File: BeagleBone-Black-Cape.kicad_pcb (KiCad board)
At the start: 4 copper layers, 61.9 x 92.1 mm, 77 parts, among them J501 Conn_ARM_JTAG_SWD_10, J502 3.3V, P101 BeagleBone_Black_Header, P102 BeagleBone_Black_Header, U401 LM3671, U601 cc1352p, U602 MX25R8035FZUIL0, Y601 32.768kHz, Y602 48MHz

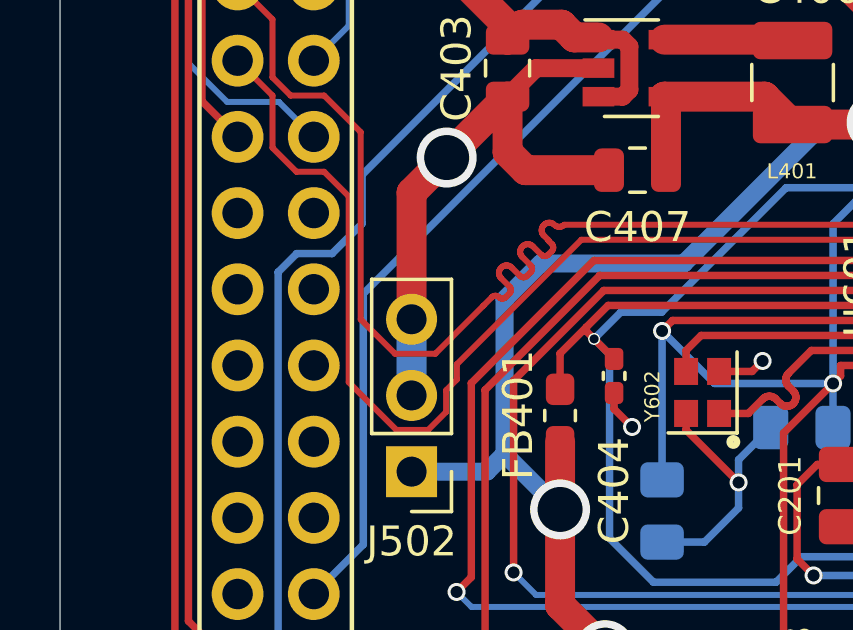
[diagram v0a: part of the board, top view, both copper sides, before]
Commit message: Made ZNP_RX trace prettier
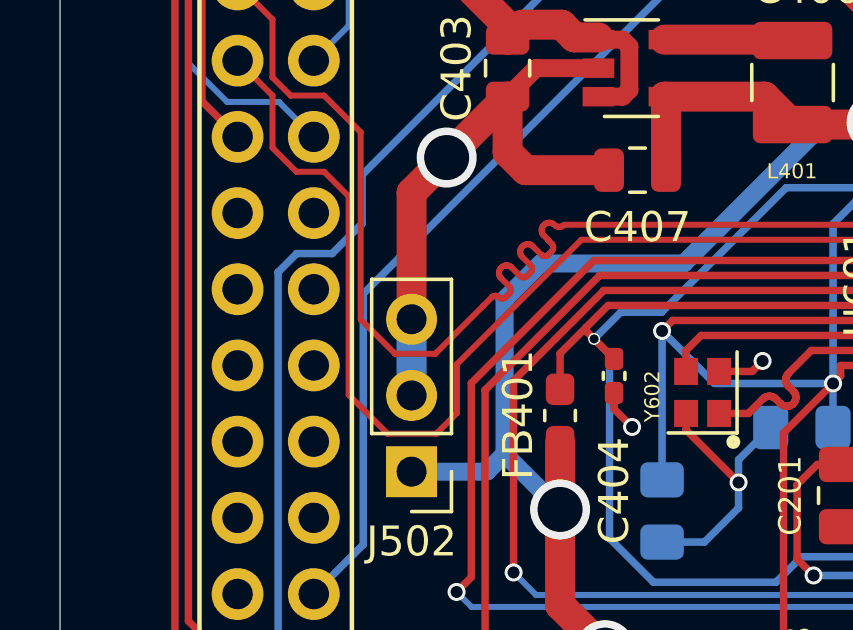
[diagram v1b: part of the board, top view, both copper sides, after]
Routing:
- net ZNP_RX: track 49.8 -> 50.3 mm
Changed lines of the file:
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@@
     (thickness 1.6)
     (drawings 22)
-    (tracks 923)
+    (tracks 921)
     (zones 0)
     (modules 77)
@@
   (segment (start 141.5201 126.6824) (end 144.4701 126.6824) (width 1) (layer F.Cu) (net 26) (status 30))
   (segment (start 152.6451 126.7074) (end 155.5951 126.7074) (width 1) (layer F.Cu) (net 26) (status 30))
-  (segment (start 127.8301 83.5924) (end 137.4401 83.5924) (width 0.2) (layer F.Cu) (net 8))
-  (segment (start 117.533701 78.786001) (end 117.533701 80.526001) (width 0.2) (layer F.Cu) (net 8))
-  (segment (start 120.073701 88.340929) (end 121.665173 89.932401) (width 0.2) (layer F.Cu) (net 8))
-  (segment (start 123.6801 87.7424) (end 127.8301 83.5924) (width 0.2) (layer F.Cu) (net 8))
-  (segment (start 117.533701 80.526001) (end 118.333701 81.326001) (width 0.2) (layer F.Cu) (net 8))
-  (segment (start 116.3701 77.6224) (end 117.533701 78.786001) (width 0.2) (layer F.Cu) (net 8) (status 10))
-  (segment (start 119.255831 81.326001) (end 120.073701 82.143871) (width 0.2) (layer F.Cu) (net 8))
-  (segment (start 122.722101 89.932401) (end 123.320101 89.334401) (width 0.2) (layer F.Cu) (net 8))
-  (segment (start 118.333701 81.326001) (end 119.255831 81.326001) (width 0.2) (layer F.Cu) (net 8))
-  (segment (start 120.073701 82.143871) (end 120.073701 88.340929) (width 0.2) (layer F.Cu) (net 8))
-  (segment (start 121.665173 89.932401) (end 122.722101 89.932401) (width 0.2) (layer F.Cu) (net 8))
-  (segment (start 123.320101 88.611345) (end 123.6801 88.251346) (width 0.2) (layer F.Cu) (net 8))
-  (segment (start 123.320101 89.334401) (end 123.320101 88.611345) (width 0.2) (layer F.Cu) (net 8))
-  (segment (start 123.6801 88.251346) (end 123.6801 87.7424) (width 0.2) (layer F.Cu) (net 8))
   (segment (start 146.558102 86.394398) (end 146.558102 85.454398) (width 0.25) (layer B.Cu) (net 8))
   (segment (start 137.4401 85.477402) (end 140.395098 88.4324) (width 0.25) (layer B.Cu) (net 8))
@@
   (segment (start 146.705099 85.307401) (end 146.7301 85.307401) (width 0.25) (layer B.Cu) (net 8))
   (segment (start 137.4401 85.477402) (end 137.4401 83.617401) (width 0.25) (layer B.Cu) (net 8))
+  (segment (start 123.6801 87.7424) (end 127.8301 83.5924) (width 0.2) (layer F.Cu) (net 8))
+  (segment (start 122.9951 90.0574) (end 123.6801 89.3724) (width 0.2) (layer F.Cu) (net 8))
+  (segment (start 121.3701 90.0574) (end 122.9951 90.0574) (width 0.2) (layer F.Cu) (net 8))
+  (segment (start 127.8301 83.5924) (end 137.4401 83.5924) (width 0.2) (layer F.Cu) (net 8))
+  (segment (start 120.073701 88.761001) (end 121.3701 90.0574) (width 0.2) (layer F.Cu) (net 8))
+  (segment (start 119.255831 81.326001) (end 120.073701 82.143871) (width 0.2) (layer F.Cu) (net 8))
+  (segment (start 120.073701 82.143871) (end 120.073701 88.761001) (width 0.2) (layer F.Cu) (net 8))
+  (segment (start 118.333701 81.326001) (end 119.255831 81.326001) (width 0.2) (layer F.Cu) (net 8))
+  (segment (start 123.6801 89.3724) (end 123.6801 87.7424) (width 0.2) (layer F.Cu) (net 8))
+  (segment (start 117.533701 80.526001) (end 118.333701 81.326001) (width 0.2) (layer F.Cu) (net 8))
+  (segment (start 117.533701 78.786001) (end 117.533701 80.526001) (width 0.2) (layer F.Cu) (net 8))
+  (segment (start 116.3701 77.6224) (end 117.533701 78.786001) (width 0.2) (layer F.Cu) (net 8))
   (via (at 146.7301 84.7824) (size 0.4) (drill 0.3) (layers F.Cu B.Cu) (net 152))
   (segment (start 145.3576 84.7824) (end 146.7301 84.7824) (width 0.2) (layer F.Cu) (net 152) (status 10))

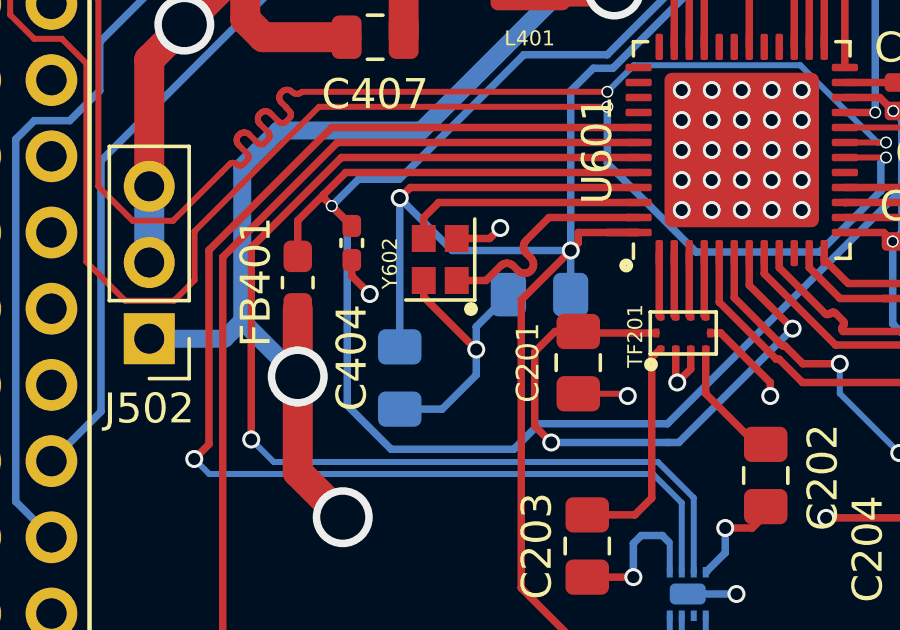
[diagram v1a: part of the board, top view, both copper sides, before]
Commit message: undid the Y602 Pad thing after crossreferencing datasheet
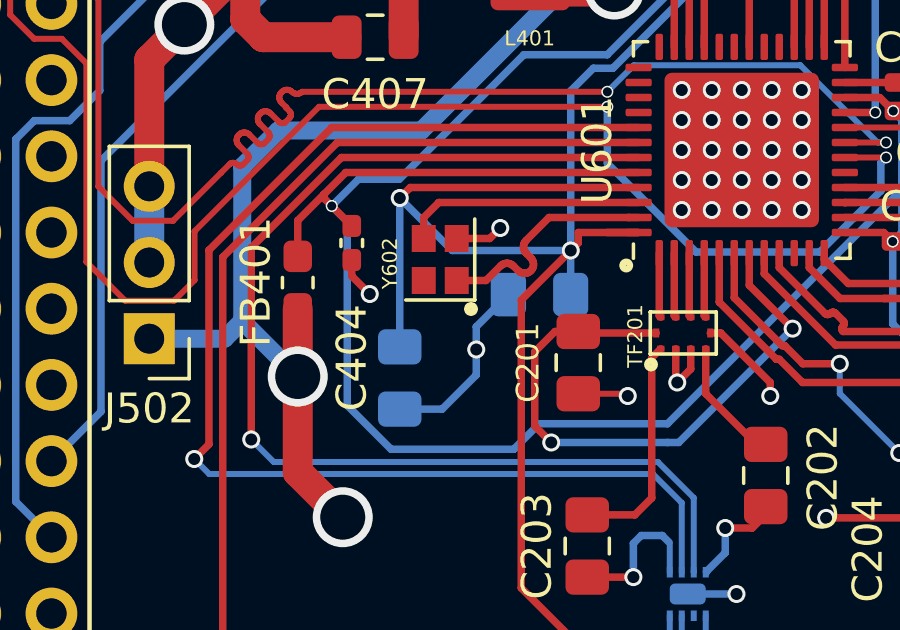
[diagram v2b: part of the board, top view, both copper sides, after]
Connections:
- Y602 pad 4: GND -> (no net)
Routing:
- net GND: track 182.1 -> 179.0 mm
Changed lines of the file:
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@@
     (thickness 1.6)
     (drawings 22)
-    (tracks 921)
+    (tracks 919)
     (zones 0)
     (modules 77)
@@
       (effects (font (size 0.5 0.5) (thickness 0.075)))
     )
-    (pad 4 smd rect (at -0.7 -0.55 90) (size 0.9 0.8) (layers F.Cu F.Paste F.Mask)
-      (net 26 GND))
+    (pad 4 smd rect (at -0.7 -0.55 90) (size 0.9 0.8) (layers F.Cu F.Paste F.Mask))
     (pad 3 smd rect (at 0.7 -0.55 90) (size 0.9 0.8) (layers F.Cu F.Paste F.Mask)
       (net 33 X48M_N))
@@
   (segment (start 116.3701 115.7224) (end 118.9101 115.7224) (width 1) (layer F.Cu) (net 26) (status 30))
   (segment (start 116.3701 118.2624) (end 118.9101 118.2624) (width 1) (layer F.Cu) (net 26) (status 30))
-  (segment (start 131.3201 89.9324) (end 133.0701 91.6824) (width 0.25) (layer F.Cu) (net 26))
-  (segment (start 131.3201 89.3824) (end 131.3201 89.9324) (width 0.25) (layer F.Cu) (net 26))
   (segment (start 138.3251 82.2074) (end 137.4401 83.0924) (width 0.2) (layer B.Cu) (net 152))
   (segment (start 143.872258 82.2074) (end 138.3251 82.2074) (width 0.2) (layer B.Cu) (net 152))

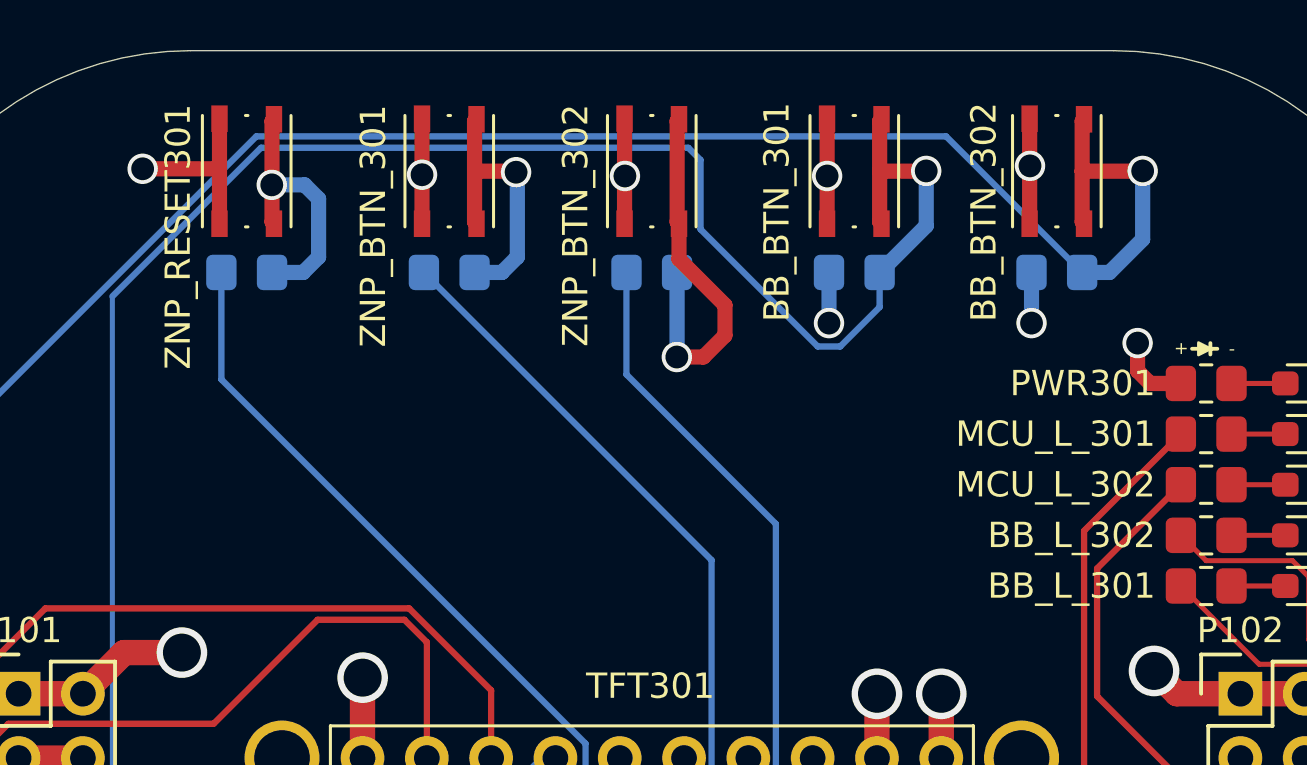
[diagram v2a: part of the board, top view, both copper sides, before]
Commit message: Fixed silkscreens for buttons and LEDs
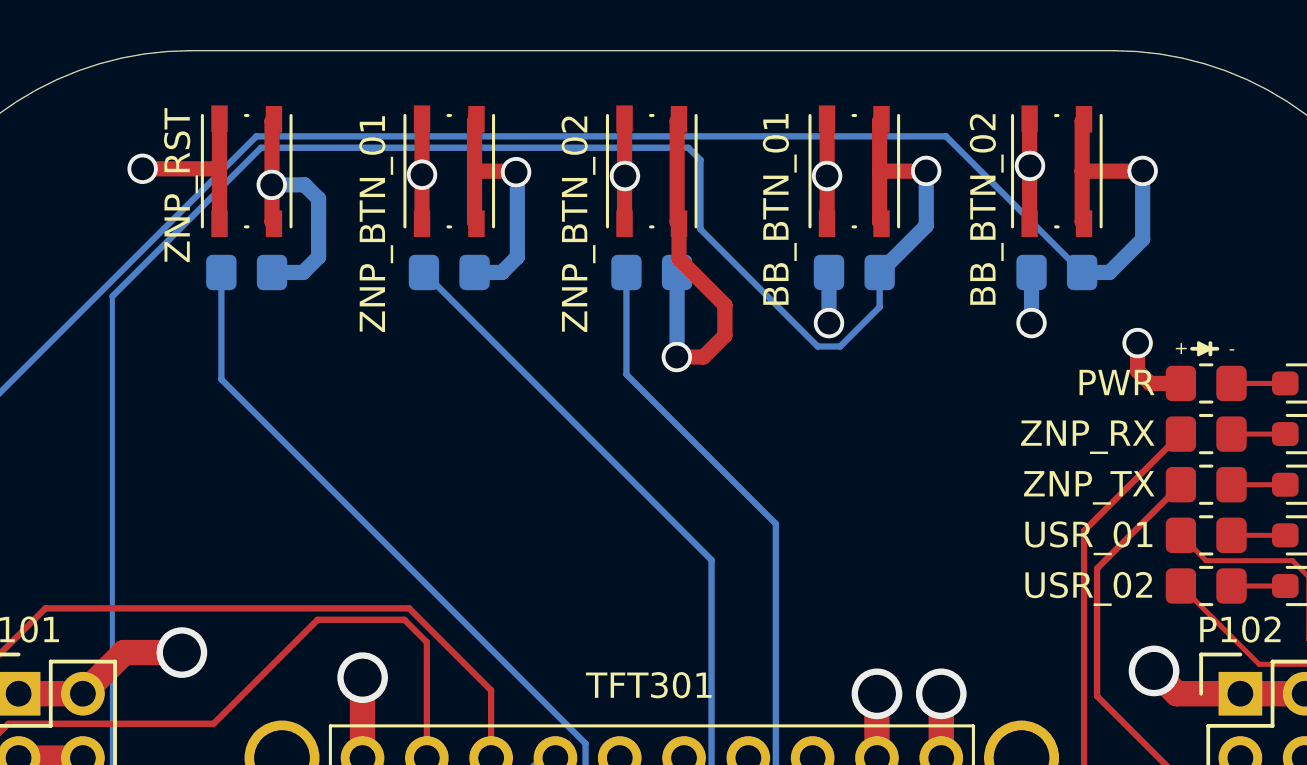
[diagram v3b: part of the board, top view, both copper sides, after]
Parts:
- renumbered BB_BTN_301 to BB_BTN_01, BB_BTN_302 to BB_BTN_02, PWR301 to PWR, BB_L_302 to USR_01, BB_L_301 to USR_02, ZNP_BTN_301 to ZNP_BTN_01, ZNP_BTN_302 to ZNP_BTN_02, ZNP_RESET301 to ZNP_RST, MCU_L_301 to ZNP_RX, MCU_L_302 to ZNP_TX
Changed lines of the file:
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@@
     (tags "tactile switch Wurth Wuerth")
     (attr smd)
-    (fp_text reference ZNP_BTN_302 (at -2.14 -3.01 90) (layer F.SilkS)
-      (effects (font (size 1 1) (thickness 0.15)))
+    (fp_text reference ZNP_BTN_02 (at -6.415 -3.01 90) (layer F.SilkS)
+      (effects (font (size 1 1) (thickness 0.15)) (justify left))
     )
     (fp_text value SW_Push (at 0 2.55 90) (layer F.Fab)
@@
     (tags "tactile switch Wurth Wuerth")
     (attr smd)
-    (fp_text reference ZNP_BTN_301 (at -2.165 -3 90) (layer F.SilkS)
-      (effects (font (size 1 1) (thickness 0.15)))
+    (fp_text reference ZNP_BTN_01 (at -6.415 -3 90) (layer F.SilkS)
+      (effects (font (size 1 1) (thickness 0.15)) (justify left))
     )
     (fp_text value SW_Push (at 0 2.55 90) (layer F.Fab)
@@
     (tags "tactile switch Wurth Wuerth")
     (attr smd)
-    (fp_text reference BB_BTN_302 (at -1.615 -2.885 90) (layer F.SilkS)
-      (effects (font (size 1 1) (thickness 0.15)))
+    (fp_text reference BB_BTN_02 (at -5.415 -2.885 90) (layer F.SilkS)
+      (effects (font (size 1 1) (thickness 0.15)) (justify left))
     )
     (fp_text value SW_Push (at 0 2.55 90) (layer F.Fab)
@@
     (tags "tactile switch Wurth Wuerth")
     (attr smd)
-    (fp_text reference BB_BTN_301 (at -1.615 -3.06 90) (layer F.SilkS)
-      (effects (font (size 1 1) (thickness 0.15)))
+    (fp_text reference BB_BTN_01 (at -5.415 -3.06 90) (layer F.SilkS)
+      (effects (font (size 1 1) (thickness 0.15)) (justify left))
     )
     (fp_text value SW_Push (at 0 2.55 90) (layer F.Fab)
@@
     (tags "LED handsolder")
     (attr smd)
-    (fp_text reference PWR301 (at 6 0) (layer F.SilkS)
+    (fp_text reference PWR (at 6 0) (layer F.SilkS)
       (effects (font (size 1 1) (thickness 0.15)) (justify right))
     )
@@
     (tags "LED handsolder")
     (attr smd)
-    (fp_text reference MCU_L_302 (at 6 0) (layer F.SilkS)
+    (fp_text reference ZNP_TX (at 6 0) (layer F.SilkS)
       (effects (font (size 1 1) (thickness 0.15)) (justify right))
     )
@@
     (tags "LED handsolder")
     (attr smd)
-    (fp_text reference MCU_L_301 (at 6 0) (layer F.SilkS)
+    (fp_text reference ZNP_RX (at 6 0) (layer F.SilkS)
       (effects (font (size 1 1) (thickness 0.15)) (justify right))
     )
@@
     (tags "LED handsolder")
     (attr smd)
-    (fp_text reference BB_L_302 (at 6 0) (layer F.SilkS)
+    (fp_text reference USR_01 (at 6 0) (layer F.SilkS)
       (effects (font (size 1 1) (thickness 0.15)) (justify right))
     )
@@
     (tags "LED handsolder")
     (attr smd)
-    (fp_text reference BB_L_301 (at 6 0) (layer F.SilkS)
+    (fp_text reference USR_02 (at 6 0) (layer F.SilkS)
       (effects (font (size 1 1) (thickness 0.15)) (justify right))
     )
@@
     (tags "tactile switch Wurth Wuerth")
     (attr smd)
-    (fp_text reference ZNP_RESET301 (at -2.59 -2.71 90) (layer F.SilkS)
-      (effects (font (size 1 1) (thickness 0.15)))
+    (fp_text reference ZNP_RST (at -3.653095 -2.71 90) (layer F.SilkS)
+      (effects (font (size 1 1) (thickness 0.15)) (justify left))
     )
     (fp_text value 612-LL3303F065QG (at 0 2.55 90) (layer F.Fab)

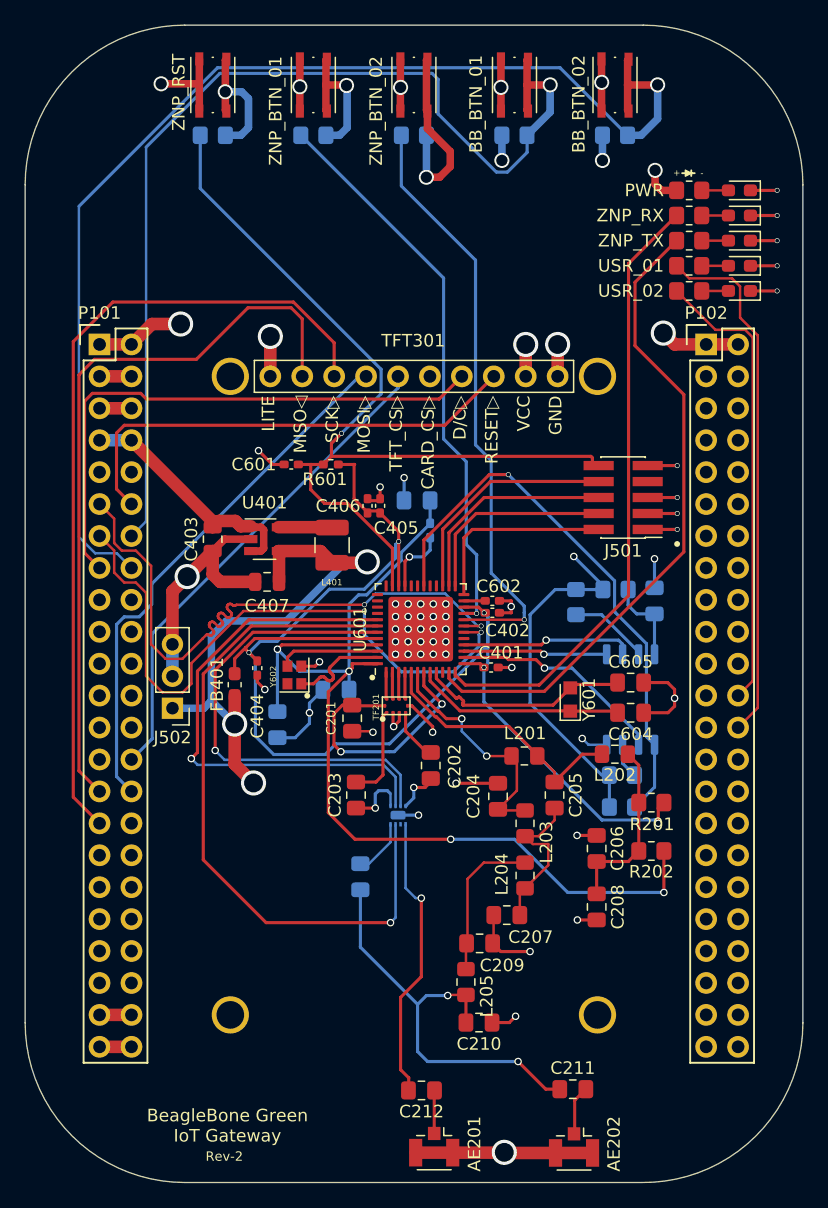
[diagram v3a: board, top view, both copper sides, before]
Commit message: resolved DRC issues. Tyler check done. Awaiting 2/3 checks
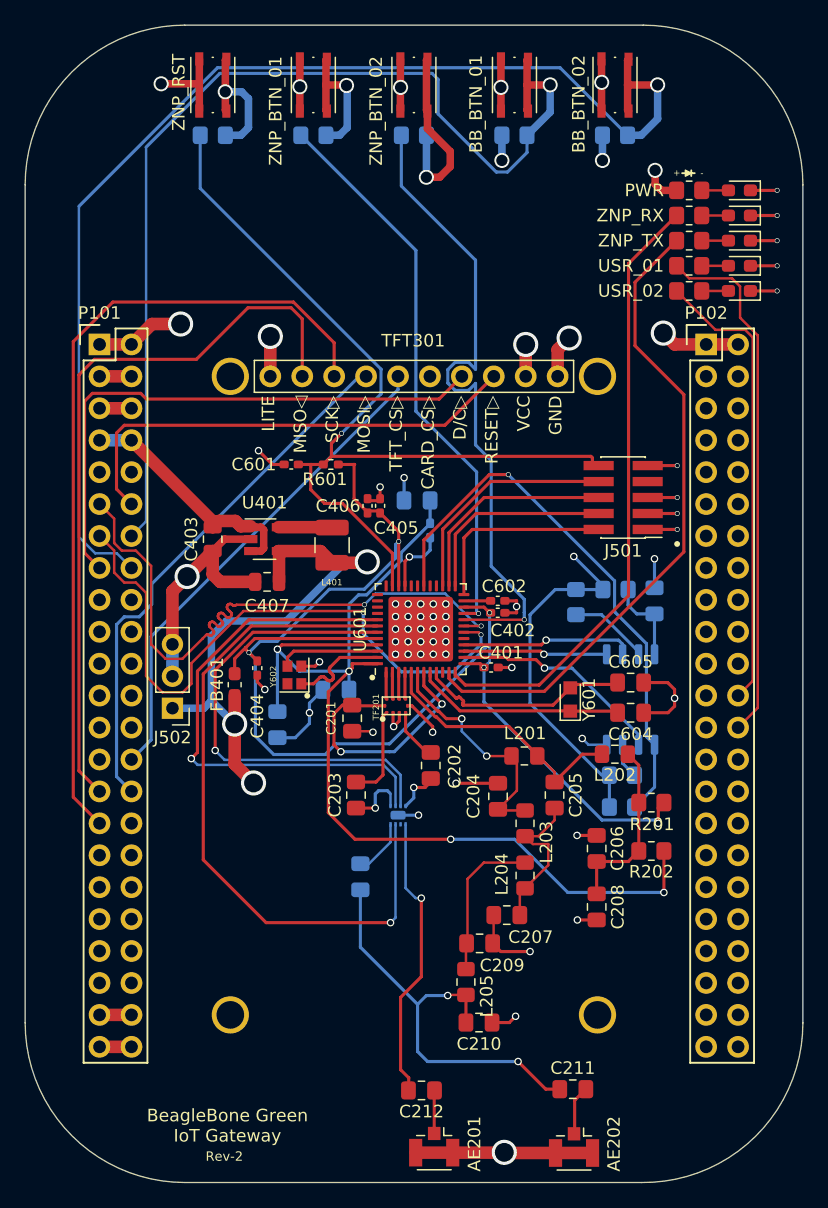
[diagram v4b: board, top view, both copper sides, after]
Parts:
- moved C402 0.43 mm to (148.1, 83.7)
- moved C602 0.43 mm to (148.1, 82.8)
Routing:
- net MCU_BTN_2: track 47.4 -> 52.7 mm
- net VDDS: track 106.5 -> 104.8 mm
- net GND: track 179.0 -> 179.9 mm
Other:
- net class Default: clearance 0.2 -> 0.127
- rule trace_clearance: 0.2 -> 0.127

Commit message: Went over things with Smoak again. Small revisions
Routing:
- net MCU_BTN_2: track 52.7 -> 47.6 mm

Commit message: Last minute fixes before staging for public
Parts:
- L205: footprint Inductor_SMD:L_0805_2012Metric_Pad1.15x1.40mm_HandSolder -> Inductor_SMD:L_0603_1608Metric_Pad1.05x0.95mm_HandSolder
- L402: footprint Inductor_SMD:L_0402_1005Metric_Pad0.77x0.64mm_HandSolder -> Inductor_SMD:L_0603_1608Metric_Pad1.05x0.95mm_HandSolder
- moved L402 0.42 mm to (142.7, 77.6)
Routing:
- net DCDC_SW: track 5.35 -> 4.58 mm
